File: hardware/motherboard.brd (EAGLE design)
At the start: 146.5 x 84 mm, 66 parts, among them IC1 7805T, Q1 16MHz, U1 ATMEGA328P-PU, U2 L293NE, U3 QRE1113, U4 QRE1113, U5 QRE1113, U6 QRE1113, U7 QRE1113, U8 QRE1113, U9 QRE1113

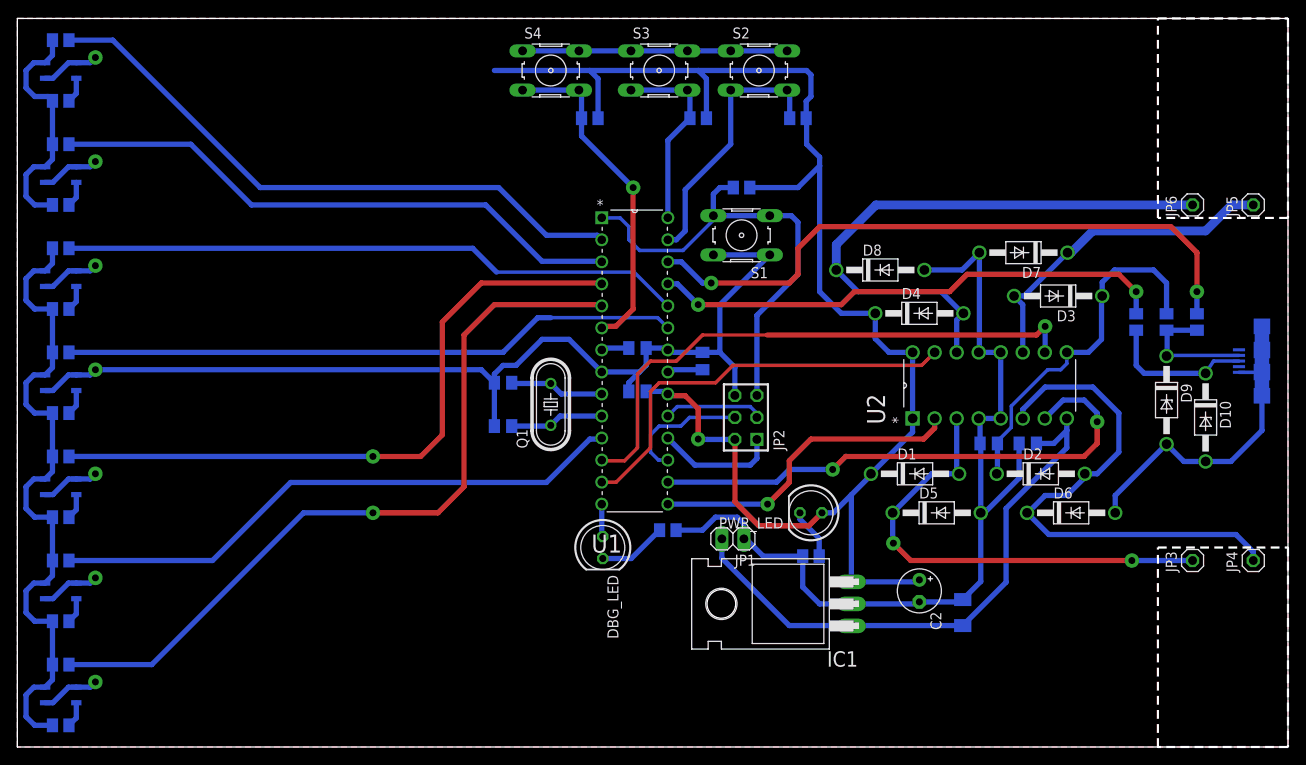
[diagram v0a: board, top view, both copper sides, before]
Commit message: Added pin header to motherboard. Fixed all wire connection from motherboard.
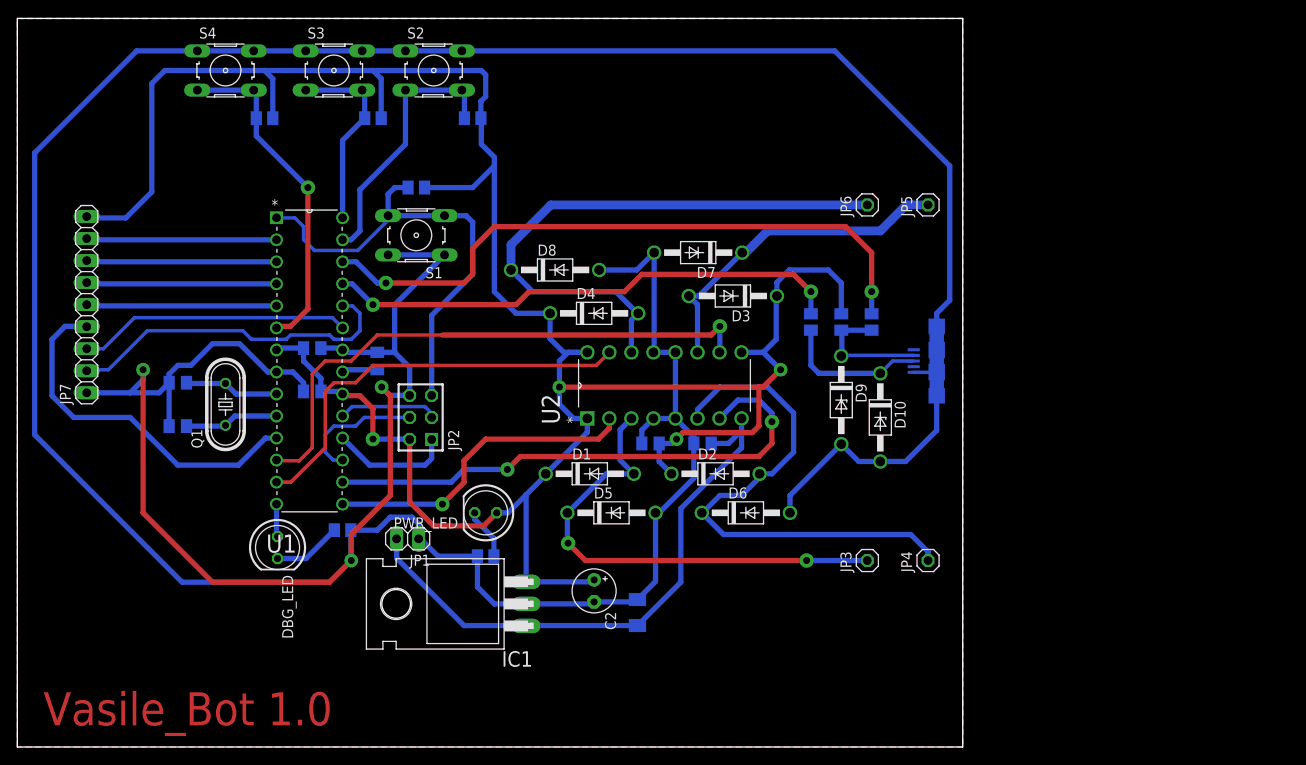
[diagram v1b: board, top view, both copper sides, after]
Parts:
- removed R10, R12, R14, R16, R4, R6, R8: 100, resistor:M0805
- removed R11, R13, R15, R17, R5, R7, R9: 220, resistor:M0805
- removed U3, U4, U5, U6, U7, U8, U9: QRE1113, SparkFun-Sensors:QRE1113
- added JP7: (no value), pinhead:1X09
- moved C9 39.0 mm to (73.0, 35.0)
- moved C1 37.5 mm to (71.5, 15.5)
- moved C2 37.5 mm to (66.5, 18.0)
- moved C3 37.5 mm to (18.5, 42.0)
- moved C4 37.5 mm to (18.5, 37.0)
- moved C5 37.5 mm to (34.0, 46.0)
- moved C6 37.5 mm to (34.0, 41.0)
- moved C7 37.5 mm to (41.5, 44.5)
- moved C8 37.5 mm to (79.0, 35.0)
- moved D1 37.5 mm to (66.0, 31.5)
- moved D10 37.5 mm to (99.5, 38.0)
- moved D2 37.5 mm to (80.5, 31.5)
- moved D3 37.5 mm to (82.5, 52.0)
- moved D4 37.5 mm to (66.5, 50.0)
- moved D5 37.5 mm to (68.5, 27.0)
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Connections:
- removed net N$10: R8.2, U4.1
- removed net N$11: R10.2, U5.1
- removed net N$12: R12.2, U6.1
- removed net N$13: R14.2, U8.1
- removed net N$14: R16.2, U9.1
- removed net N$8: R4.2, U7.1
- removed net N$9: R6.2, U3.1
- net GND: now also JP7.1; no longer U3.2, U3.4, U4.2, U4.4, U5.2, U5.4, U6.2, U6.4, U7.2, U7.4, U8.2, U8.4, U9.2, U9.4
- net S1: now also JP7.8; no longer R5.1
- net S2: now also JP7.7; no longer R7.1
- net S3: now also JP7.6; no longer R11.1
- net S4: now also JP7.5; no longer R9.1
- net S5: now also JP7.4; no longer R13.1
- net S6: now also JP7.3; no longer R15.1
- net S7: now also JP7.2; no longer R17.1
- net VCC: now also JP7.9; no longer R10.1, R11.2, R12.1, R13.2, R14.1, R15.2, R16.1, R17.2, R4.1, R5.2, R6.1, R7.2, R8.1, R9.2, U3.3, U4.3, U5.3, U6.3, U7.3, U8.3, U9.3
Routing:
- net GND: track 333.8 -> 499.1 mm, vias 7 -> 3
- net S4: track 88.9 -> 21.9 mm, vias 1 -> 0
- net S3: track 77.4 -> 21.9 mm, vias 1 -> 0
- net S1: track 71.0 -> 21.9 mm
- net S2: track 67.0 -> 21.9 mm
- net S6: track 71.2 -> 31.5 mm
- net VCC: track 324.1 -> 285.4 mm, vias 1 -> 4
- net S7: track 71.8 -> 39.0 mm
- net S5: track 67.3 -> 41.6 mm
- net N$12: track 2.95 -> 0.00 mm
- net N$14: track 2.95 -> 0.00 mm
- net N$13: track 2.95 -> 0.00 mm
- net N$11: track 2.95 -> 0.00 mm
- net N$10: track 2.95 -> 0.00 mm
- net N$8: track 2.95 -> 0.00 mm
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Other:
- board size 146.5 x 84 mm -> 109 x 84 mm
- board text added: "Vasile_Bot 1.0"

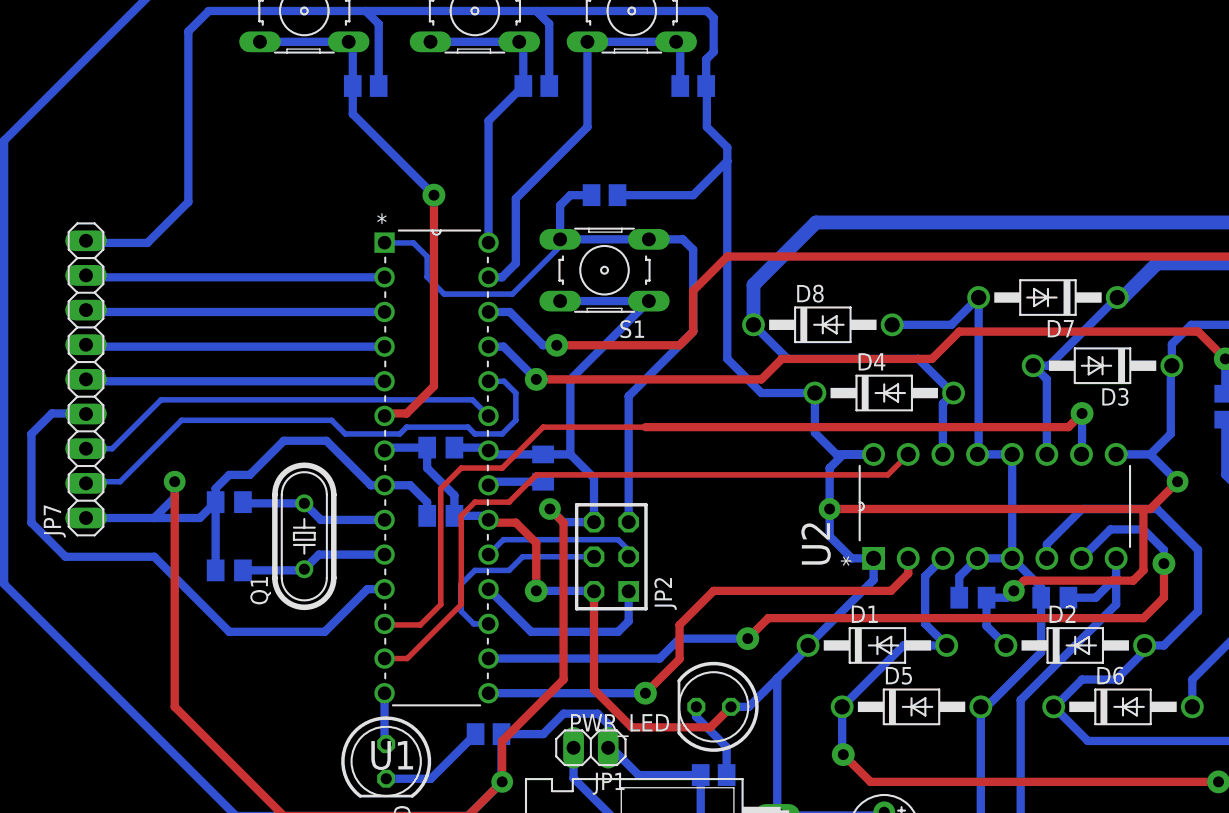
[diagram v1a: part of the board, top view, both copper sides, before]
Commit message: Added capacitors to sensor board. Fixed routing.
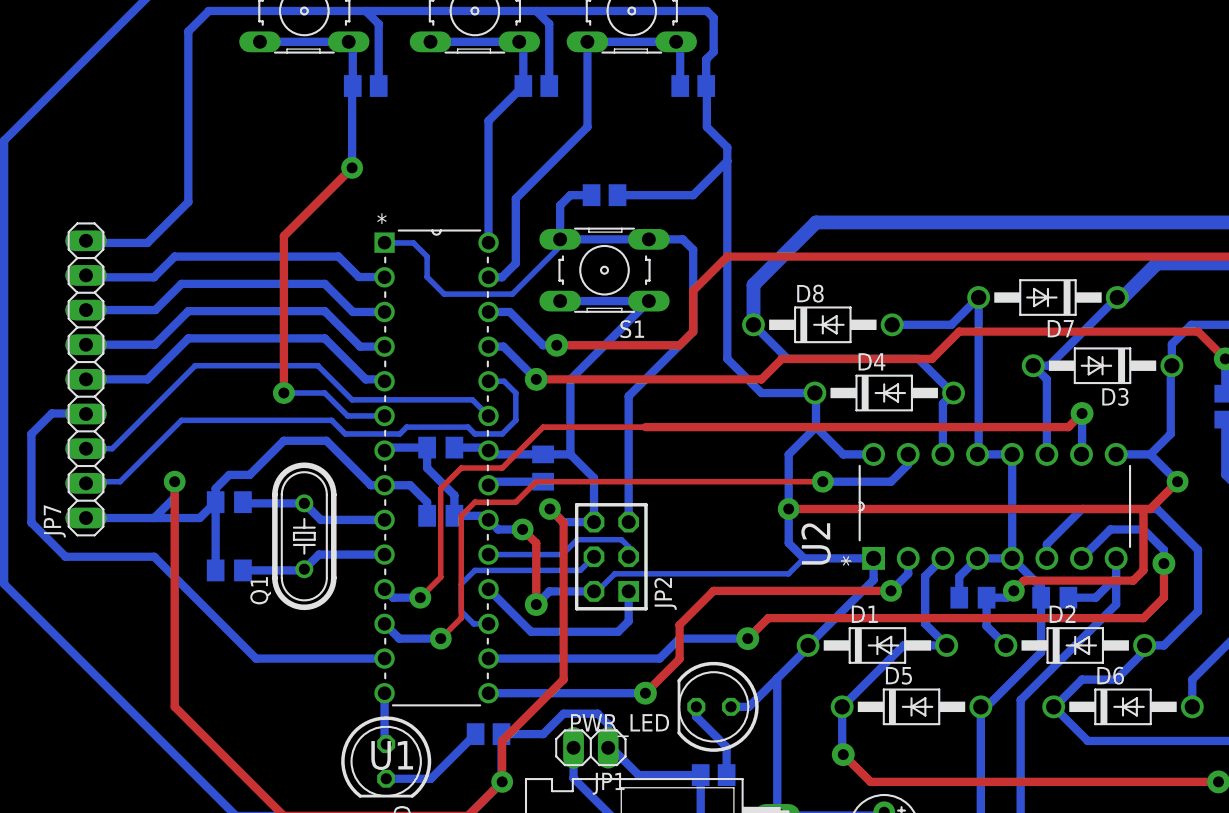
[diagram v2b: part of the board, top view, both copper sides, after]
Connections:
- net M1B: now also U1.11; no longer U1.12
- net M2B: now also U1.12; no longer U1.13
- net S5: now also U1.13; no longer U1.11
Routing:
- net VCC: track 285.4 -> 290.4 mm, vias 4 -> 5
- net BTN1: track 38.9 -> 42.5 mm, vias 1 -> 2
- net S4: track 21.9 -> 24.4 mm
- net S6: track 31.5 -> 33.5 mm
- net S3: track 21.9 -> 24.0 mm
- net M1B: track 65.6 -> 63.8 mm, vias 1 -> 2
- net S2: track 21.9 -> 23.5 mm
- net S1: track 21.9 -> 23.2 mm
- net M2B: track 48.4 -> 49.3 mm, vias 0 -> 2
- net M1A: vias 1 -> 2

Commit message: Fixed motherboard errors.
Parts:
- moved C9 7.38 mm to (69.5, 41.5), turned to 0 degrees
- moved D4 2.00 mm to (64.5, 50.0), turned to 180 degrees
- turned D1 to 180 degrees
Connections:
- net VCC: no longer D1.C, D2.C, D3.C, D4.C
- net VCC/2: now also D1.C, D2.C, D3.C, D4.C
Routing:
- net VCC/2: track 66.2 -> 114.9 mm, vias 0 -> 3
- net VCC: track 290.4 -> 270.9 mm, vias 5 -> 4
- net GND: track 499.1 -> 508.2 mm
- net N$7: track 67.5 -> 65.6 mm
- net D-: track 74.8 -> 73.0 mm
- net N$4: track 56.4 -> 57.6 mm
